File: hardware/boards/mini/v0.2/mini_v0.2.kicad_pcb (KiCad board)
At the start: 8 copper layers, 20 x 41 mm, 99 parts, among them IC1 NAU88C22YG, IC3 IS42S16160J-6BLI, J2 Top, J3 Bottom, Q1 PMV37EN22, U1 W25Q128JVP, U2 LTV-217-G, U4 STM32H750XBHx, Y1 Crystal_GND24, Y3 32.768kHz

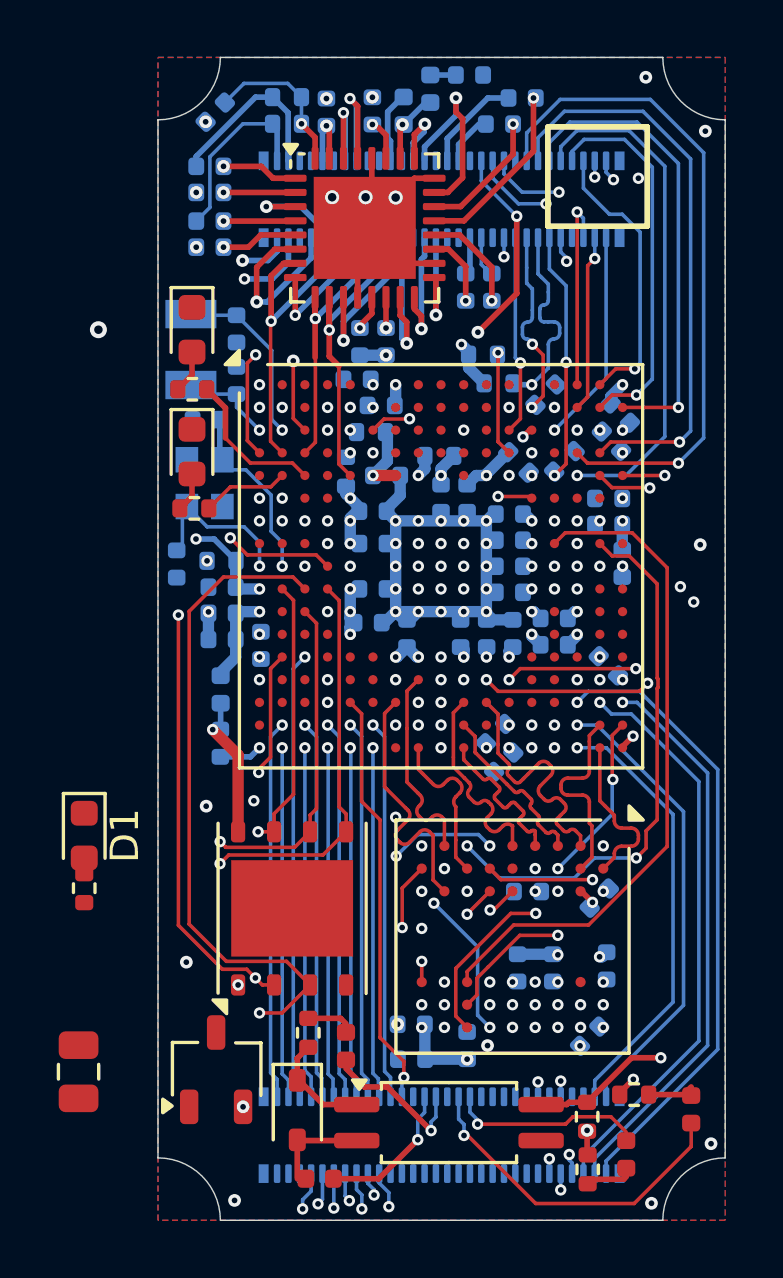
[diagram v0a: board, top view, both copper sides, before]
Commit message: mini: fix mounting bite sizing, make power input reversable without damage
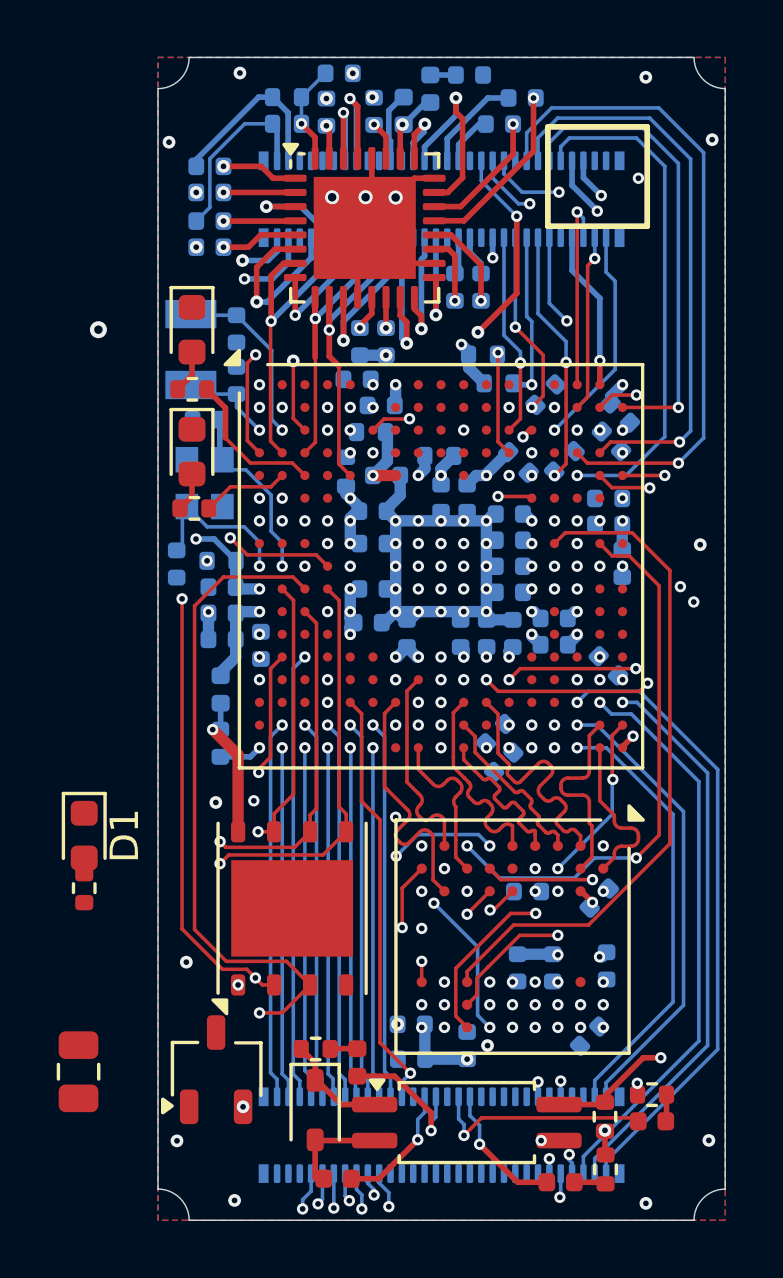
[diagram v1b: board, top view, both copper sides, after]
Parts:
- C15: value R -> C
- moved C28 4.58 mm to (76.4, 57.6), turned to 0 degrees
- moved FB5 2.51 mm to (84.2, 96.7), turned to 180 degrees
- moved FB4 1.44 mm to (87.4, 94.5), turned to 180 degrees
- moved FB2 0.70 mm to (77.0, 92.4)
- moved D3 0.63 mm to (75.5, 94.1)
- moved R6 0.63 mm to (85.8, 94.3)
- moved FB3 0.63 mm to (76.3, 96.5)
- moved R8 0.63 mm to (87.4, 93.6)
- moved R9 0.63 mm to (85.8, 96.2)
- moved U2 0.63 mm to (80.9, 94.6)
- moved R7 0.63 mm to (75.6, 92.0), turned to 180 degrees
- moved C26 0.38 mm to (81.4, 65.1)
- moved C27 0.38 mm to (80.5, 65.1)
- moved C29 0.06 mm to (77.6, 58.9)
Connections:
- J2 pad 1: /PA11/4RX -> unconnected-(J2-Pad1)
- J2 pad 10: /SDMMC1_D0 -> unconnected-(J2-Pad10)
- J2 pad 12: /SDMMC1_D1 -> /SDMMC1_D0
- J2 pad 14: /SDMMC1_D2 -> /SDMMC1_D1
- J2 pad 16: /SDMMC1_D3 -> /SDMMC1_D2
- J2 pad 18: /SDMMC1_CK -> /SDMMC1_D3
- J2 pad 20: /SDMMC1_CMD -> /SDMMC1_CK
- J2 pad 22: unconnected-(J2-Pad22) -> /SDMMC1_CMD
- J2 pad 24: /AUX_IN_R -> unconnected-(J2-Pad24)
- J2 pad 26: /AUX_IN_L -> /AUX_IN_R
- J2 pad 28: unconnected-(J2-Pad28) -> /AUX_IN_L
- J2 pad 3: /PA12/4TX -> unconnected-(J2-Pad3)
- J2 pad 5: /PI0 -> /PA11/4RX
- J2 pad 51: +3.3V -> unconnected-(J2-Pad51)
- J2 pad 7: /PH15 -> /PA12/4TX
- J2 pad 8: unconnected-(J2-Pad8) -> /SPI_NSS
- U4 pad A16: /PI0 -> /SPI_NSS
- U4 pad B16: /PH15 -> unconnected-(U4H-PH15-PadB16)
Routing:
- net /PH15: track 13.5 -> 0.00 mm, vias 1 -> 0
- net /PI0: track 9.97 -> 0.00 mm, vias 1 -> 0
- net /SPI_NSS: track 0.00 -> 5.59 mm, vias 0 -> 1
- net /DIN_OUT_SINK: track 11.8 -> 7.90 mm
- net /PK0: track 27.1 -> 29.7 mm
- net /I2C_SCL: track 12.1 -> 10.1 mm
- net Net-(IC1-MICBIAS): track 5.62 -> 3.64 mm
- net /DIN_OUT_SOURCE: track 6.65 -> 4.74 mm
- net unconnected-(U4H-PH15-PadB16): track 0.00 -> 1.47 mm, vias 0 -> 1
- net /SDMMC1_D2: track 7.16 -> 5.94 mm
- net +3.3V: track 49.5 -> 48.4 mm
- net Net-(FB4-Pad1): track 1.61 -> 0.95 mm
- net /DIN_IN_SINK: track 4.86 -> 4.23 mm
- net GND: vias 81 -> 84
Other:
- outline, holes or cut-outs redrawn

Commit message: mini: start routing remaining lower GPIO
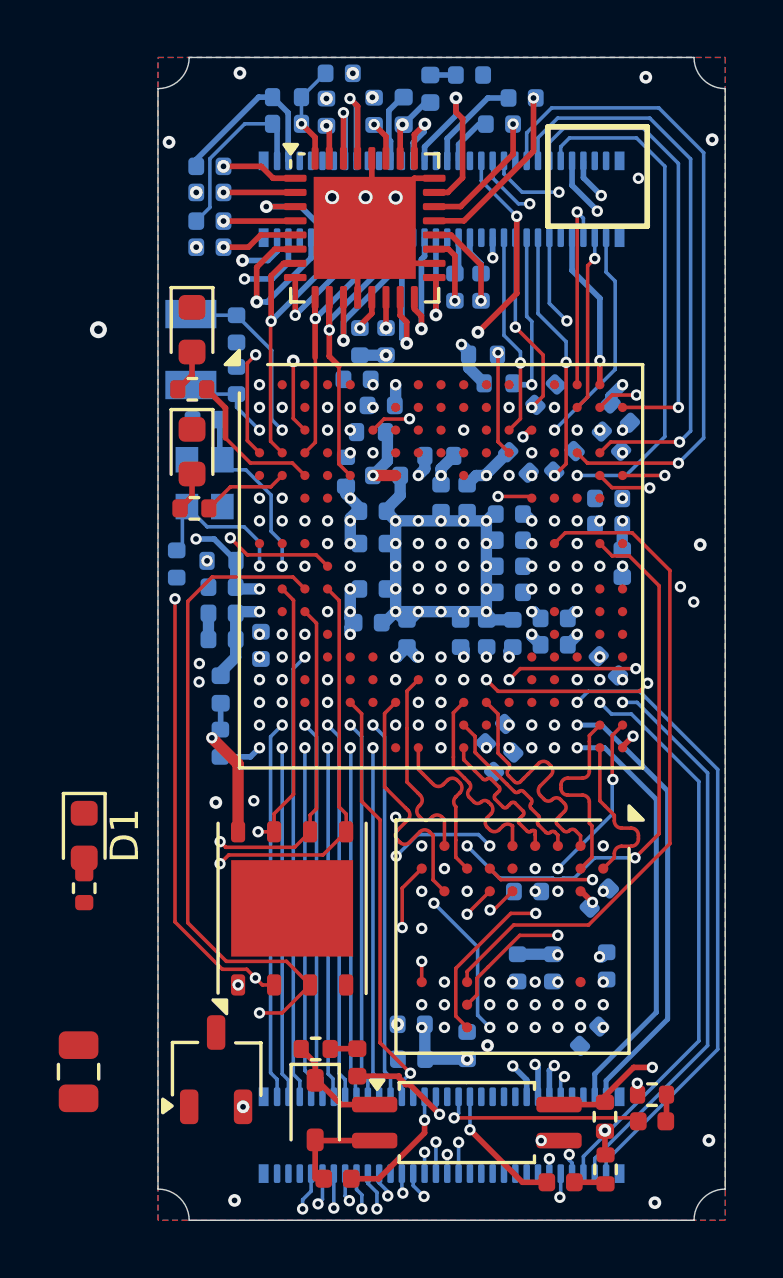
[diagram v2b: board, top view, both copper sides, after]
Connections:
- J3 pad 11: unconnected-(J3-Pad11) -> /PB13
- J3 pad 13: /PB13 -> /PH8
- J3 pad 15: unconnected-(J3-Pad15) -> /PH7
- J3 pad 17: /PH8 -> unconnected-(J3-Pad17)
- J3 pad 21: /PH7 -> unconnected-(J3-Pad21)
- J3 pad 28: unconnected-(J3-Pad28) -> /PA0
- J3 pad 30: unconnected-(J3-Pad30) -> /PC3
- J3 pad 32: unconnected-(J3-Pad32) -> /PC2_C
- J3 pad 34: unconnected-(J3-Pad34) -> /PH3
- J3 pad 36: unconnected-(J3-Pad36) -> /PC1
- J3 pad 38: unconnected-(J3-Pad38) -> /PC2
- U4 pad M2: unconnected-(U4C-PC1-PadM2) -> /PC1
- U4 pad M3: unconnected-(U4C-PC2-PadM3) -> /PC2
- U4 pad P2: unconnected-(U4H-PH3-PadP2) -> /PH3
- U4 pad R1: unconnected-(U4C-PC2_C-PadR1) -> /PC2_C
- U4 pad R2: unconnected-(U4C-PC3_C-PadR2) -> /PC3
- U4 pad T1: unconnected-(U4A-PA0_C-PadT1) -> /PA0
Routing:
- net /PC2: track 0.00 -> 30.4 mm, vias 0 -> 3
- net /PC1: track 0.00 -> 29.3 mm, vias 0 -> 3
- net /PH3: track 0.00 -> 21.0 mm, vias 0 -> 2
- net /PC2_C: track 0.00 -> 19.1 mm, vias 0 -> 2
- net /PC3: track 0.00 -> 18.9 mm, vias 0 -> 2
- net /PA0: track 0.00 -> 17.7 mm, vias 0 -> 2
- net /PH8: track 12.6 -> 18.5 mm, vias 1 -> 2
- net /PH7: track 12.5 -> 18.3 mm, vias 1 -> 2
- net /FMC_SDCKE0: track 15.0 -> 13.7 mm
- net /PB13: track 17.4 -> 18.4 mm
- net /DIN_IN_SOURCE: track 5.03 -> 4.16 mm
- net /DIN_OUT_SINK: track 7.90 -> 7.36 mm
- net /USB_D-: track 15.5 -> 14.9 mm
- net GND: vias 84 -> 81
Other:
- board text added: "USB differential pair is impedance matches assuming JLC08161H-2116 stackup which is {dblquote}free{dblquote} for 8-layer boards. JLC impedance tool gives: Trace width: 0.1773mil Trace spacing: 0.2mm"
